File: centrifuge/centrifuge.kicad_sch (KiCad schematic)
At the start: 0 parts

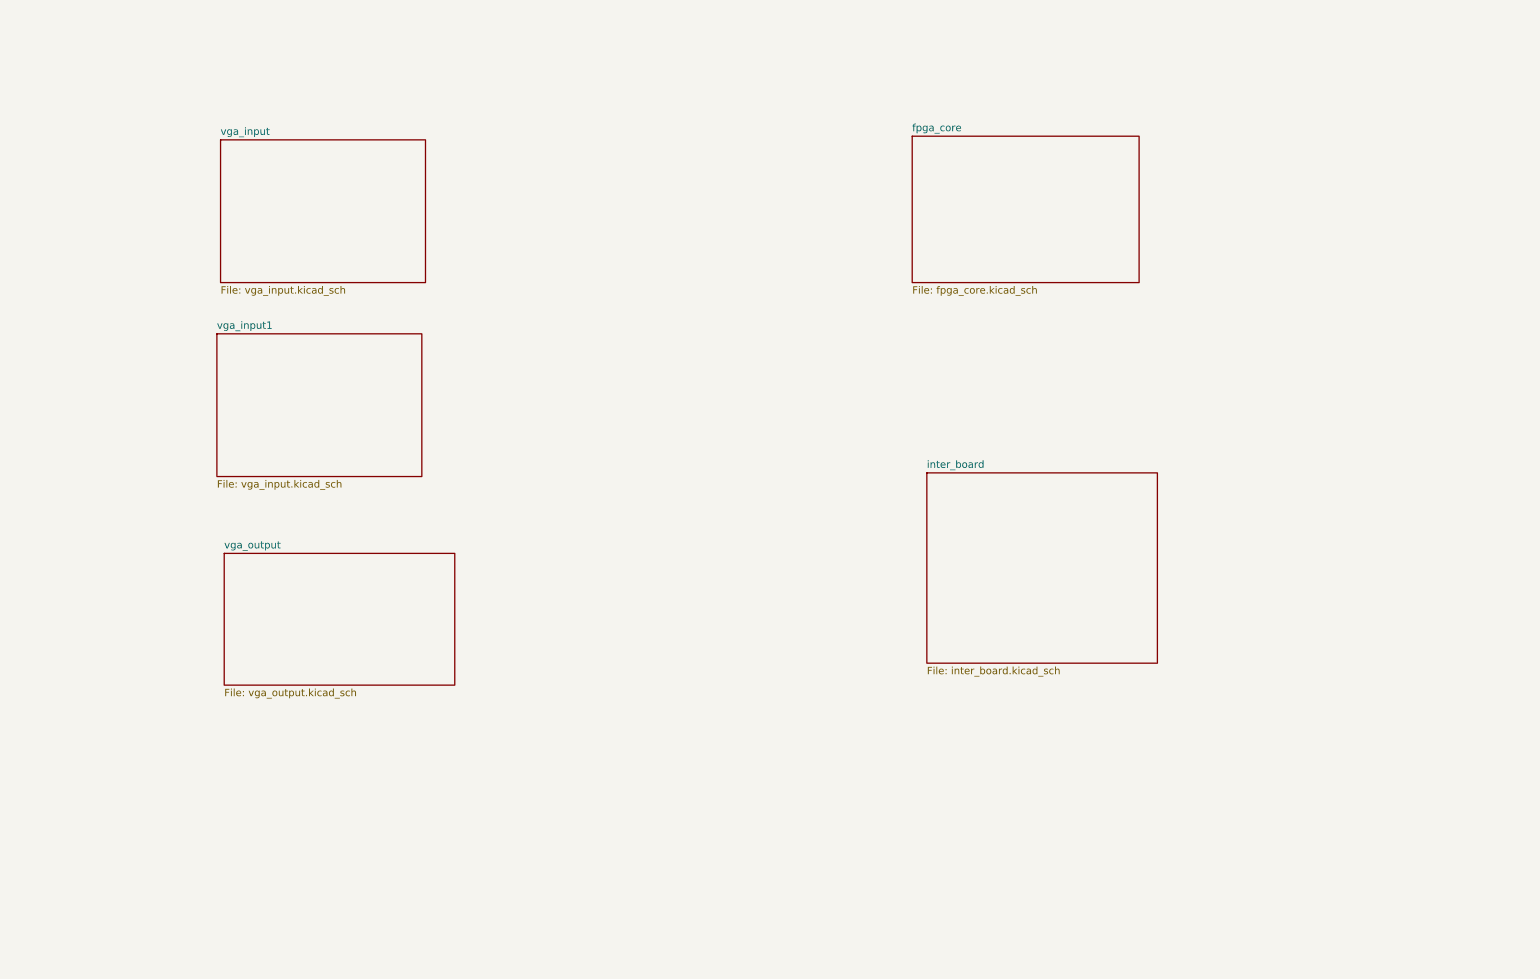
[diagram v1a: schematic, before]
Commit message: Completed majority of schematic, need to add decoupling but otherwise mostly ready
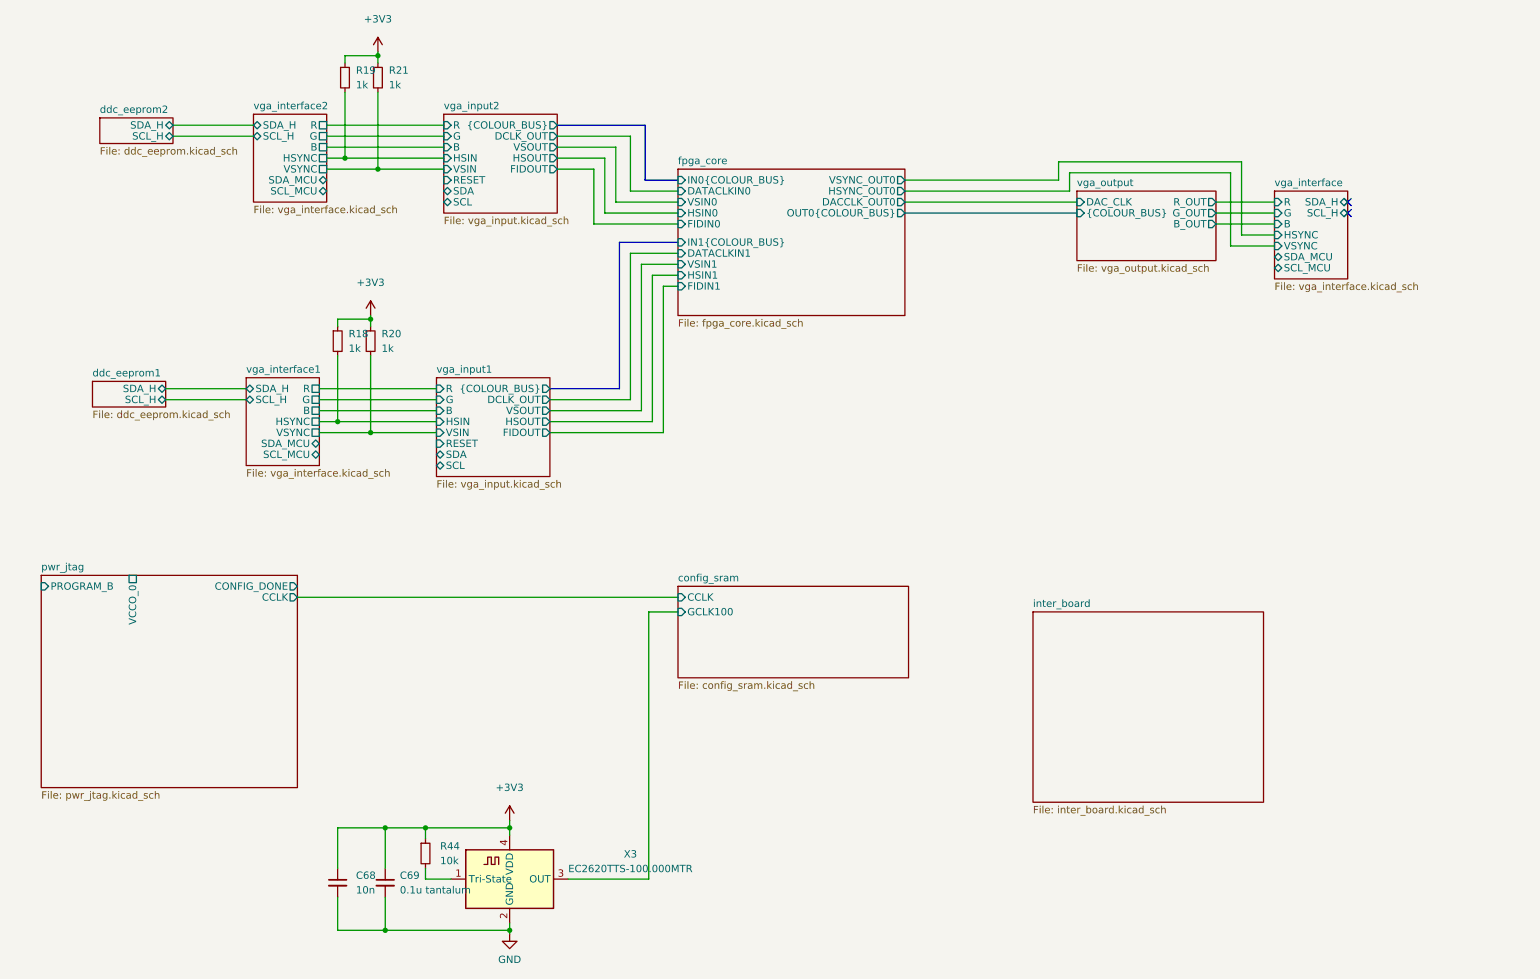
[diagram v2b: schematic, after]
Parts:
- added C68: 10n, Capacitor_SMD:C_0805_2012Metric_Pad1.18x1.45mm_HandSolder, symbol Device:C_Small
- added C69: 0.1u tantalum, Capacitor_SMD:C_0805_2012Metric_Pad1.18x1.45mm_HandSolder, symbol Device:C_Small
- added R18, R19, R20, R21: 1k, Resistor_SMD:R_0805_2012Metric_Pad1.20x1.40mm_HandSolder, symbol Device:R_Small
- added R44: 10k, Resistor_SMD:R_0805_2012Metric_Pad1.20x1.40mm_HandSolder, symbol Device:R_Small
- added X3: EC2620TTS-100.000MTR, Oscillator:Oscillator_SMD_EuroQuartz_XO91-4Pin_7.0x5.0mm_HandSoldering, symbol centrifuge_symbols:EC2620TTS-100.000MTR
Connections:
- new net: R44.2, X3.1 (Tri-State)
- new net +3V3: C68.1, C69.1, R18.1, R19.1, R20.1, R21.1, R44.1, X3.4 (VDD)
- new net GND: C68.2, C69.2, X3.2 (GND)
- new net config_sram/GCLK100: X3.3 (OUT)
- new net vga_input1/HSIN: R18.2
- new net vga_input1/VSIN: R20.2
- new net vga_input2/HSIN: R19.2
- new net vga_input2/VSIN: R21.2
- no-connect marks 0 -> 2
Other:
- removed sheet vga_input
- added sheet config_sram (config_sram.kicad_sch)
- added sheet ddc_eeprom1 (ddc_eeprom.kicad_sch)
- added sheet ddc_eeprom2 (ddc_eeprom.kicad_sch)
- added sheet pwr_jtag (pwr_jtag.kicad_sch)
- added sheet vga_input2 (vga_input.kicad_sch)
- added sheet vga_interface (vga_interface.kicad_sch)
- added sheet vga_interface1 (vga_interface.kicad_sch)
- added sheet vga_interface2 (vga_interface.kicad_sch)
- sheet fpga_core ports: added DACCLK_OUT0, DATACLKIN0, DATACLKIN1, FIDIN0, FIDIN1, HSIN0, HSIN1, HSYNC_OUT0, IN0{COLOUR_BUS}, IN1{COLOUR_BUS}, OUT0{COLOUR_BUS}, VSIN0, VSIN1, VSYNC_OUT0; removed none
- sheet vga_input1 ports: added B, DCLK_OUT, FIDOUT, G, HSIN, HSOUT, R, RESET, SCL, SDA, VSIN, VSOUT, {COLOUR_BUS}; removed none
- sheet vga_output ports: added B_OUT, DAC_CLK, G_OUT, R_OUT, {COLOUR_BUS}; removed none
- title: VGA Centrifuge FPGA board -> VGA Centrifuge

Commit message: FPGA PCB design completed
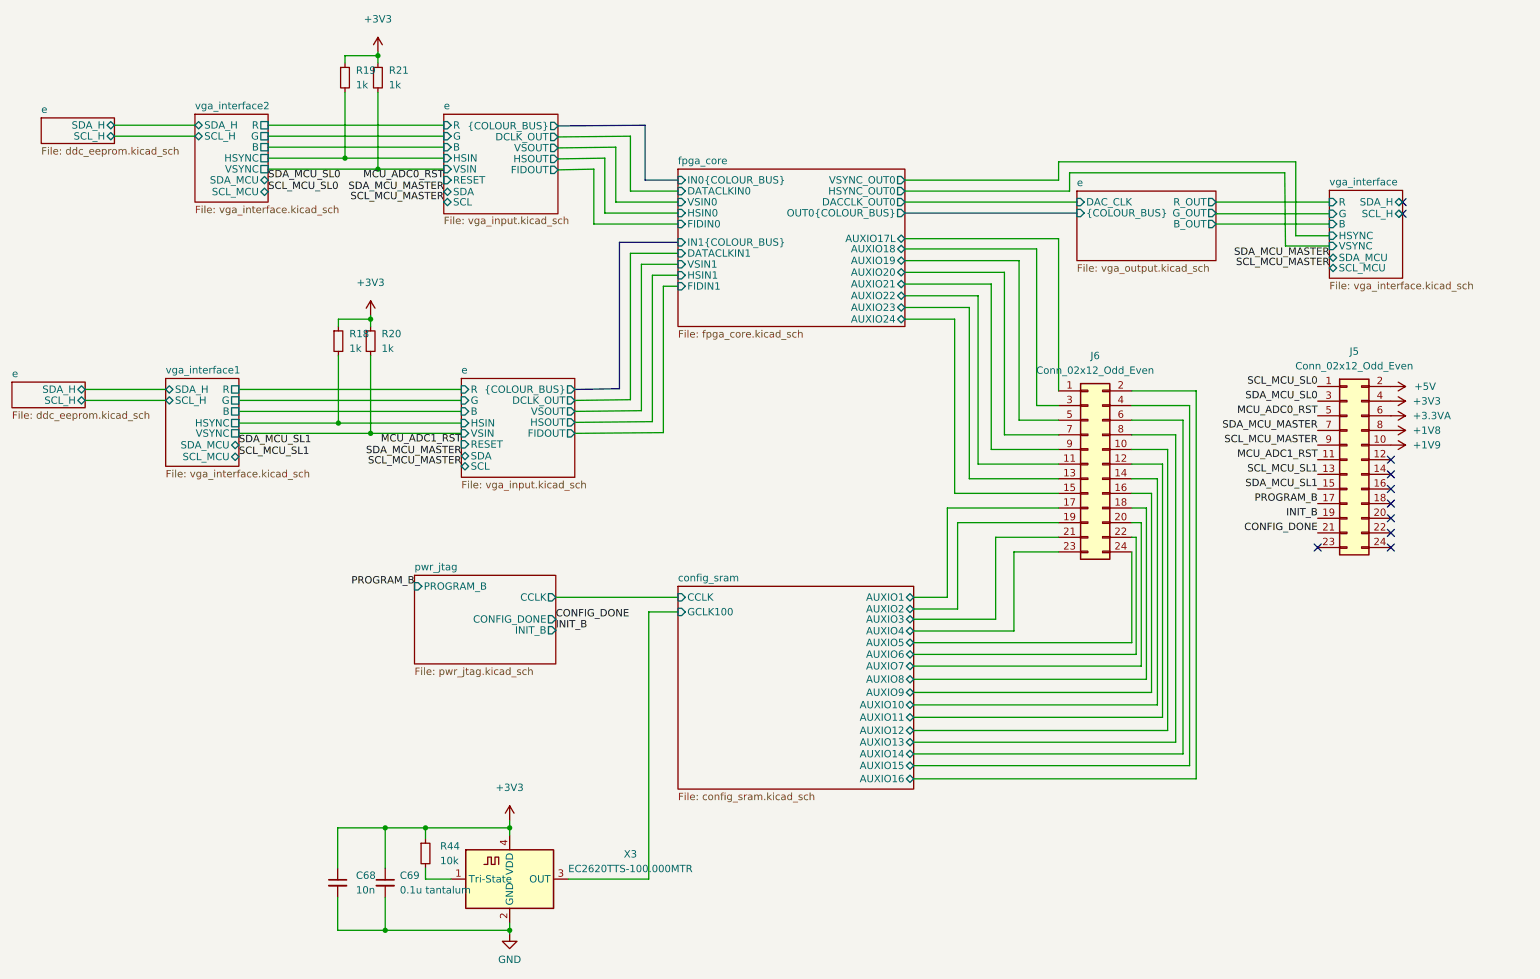
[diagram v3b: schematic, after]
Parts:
- added J5, J6: Conn_02x12_Odd_Even, Connector_PinHeader_2.54mm:PinHeader_2x12_P2.54mm_Horizontal, symbol Connector_Generic:Conn_02x12_Odd_Even
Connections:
- net +3V3: now also J5.4 (Pin_4)
- net vga_input1/HSIN renamed e/HSIN
- net vga_input1/VSIN renamed e/VSIN
- net vga_input2/HSIN renamed e/HSIN
- net vga_input2/VSIN renamed e/VSIN
- new net +1V8: J5.8 (Pin_8)
- new net +1V9: J5.10 (Pin_10)
- new net +3.3VA: J5.6 (Pin_6)
- new net +5V: J5.2 (Pin_2)
- new net CONFIG_DONE: J5.21 (Pin_21)
- new net INIT_B: J5.19 (Pin_19)
- new net MCU_ADC0_RST: J5.5 (Pin_5)
- new net MCU_ADC1_RST: J5.11 (Pin_11)
- new net PROGRAM_B: J5.17 (Pin_17)
- new net SCL_MCU_MASTER: J5.9 (Pin_9)
- new net SCL_MCU_SL0: J5.1 (Pin_1)
- new net SCL_MCU_SL1: J5.13 (Pin_13)
- new net SDA_MCU_MASTER: J5.7 (Pin_7)
- new net SDA_MCU_SL0: J5.3 (Pin_3)
- new net SDA_MCU_SL1: J5.15 (Pin_15)
- new net config_sram/AUXIO1: J6.17 (Pin_17)
- new net config_sram/AUXIO10: J6.14 (Pin_14)
- new net config_sram/AUXIO11: J6.12 (Pin_12)
- new net config_sram/AUXIO12: J6.10 (Pin_10)
- new net config_sram/AUXIO13: J6.8 (Pin_8)
- new net config_sram/AUXIO14: J6.6 (Pin_6)
- new net config_sram/AUXIO15: J6.4 (Pin_4)
- new net config_sram/AUXIO16: J6.2 (Pin_2)
- new net config_sram/AUXIO2: J6.19 (Pin_19)
- new net config_sram/AUXIO3: J6.21 (Pin_21)
- new net config_sram/AUXIO4: J6.23 (Pin_23)
- new net config_sram/AUXIO5: J6.24 (Pin_24)
- new net config_sram/AUXIO6: J6.22 (Pin_22)
- new net config_sram/AUXIO7: J6.20 (Pin_20)
- new net config_sram/AUXIO8: J6.18 (Pin_18)
- new net config_sram/AUXIO9: J6.16 (Pin_16)
- new net fpga_core/AUXIO17L: J6.1 (Pin_1)
- new net fpga_core/AUXIO18: J6.3 (Pin_3)
- new net fpga_core/AUXIO19: J6.5 (Pin_5)
- new net fpga_core/AUXIO20: J6.7 (Pin_7)
- new net fpga_core/AUXIO21: J6.9 (Pin_9)
- new net fpga_core/AUXIO22: J6.11 (Pin_11)
- new net fpga_core/AUXIO23: J6.13 (Pin_13)
- new net fpga_core/AUXIO24: J6.15 (Pin_15)
- no-connect marks 2 -> 10
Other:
- sheet ddc_eeprom1 renamed e
- removed sheet ddc_eeprom2
- removed sheet inter_board
- removed sheet vga_input1
- removed sheet vga_input2
- removed sheet vga_output
- sheet config_sram ports: added AUXIO1, AUXIO10, AUXIO11, AUXIO12, AUXIO13, AUXIO14, AUXIO15, AUXIO16, AUXIO2, AUXIO3, AUXIO4, AUXIO5, AUXIO6, AUXIO7, AUXIO8, AUXIO9; removed none
- sheet fpga_core ports: added AUXIO17L, AUXIO18, AUXIO19, AUXIO20, AUXIO21, AUXIO22, AUXIO23, AUXIO24; removed none
- sheet pwr_jtag ports: added INIT_B; removed VCCO_0
